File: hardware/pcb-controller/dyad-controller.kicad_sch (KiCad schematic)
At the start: 41 parts, among them J1 USB_C_Receptacle_USB2.0, J10 USB-C split link, J2 SWD, J6 HC-FPC-0.5-20P-FH20, J7 HC-FPC-0.5-20P-FH20, J8 HC-FPC-0.5-14P-FH20, J9 USB-C split link, SW1 BOOTSEL, SW2 RESET, U1 W25Q128JVS, U2 USBLC6-2SC6, U3 RP2040, U4 XC6206PxxxMR-Regulator_Linear, Y1 12MHz

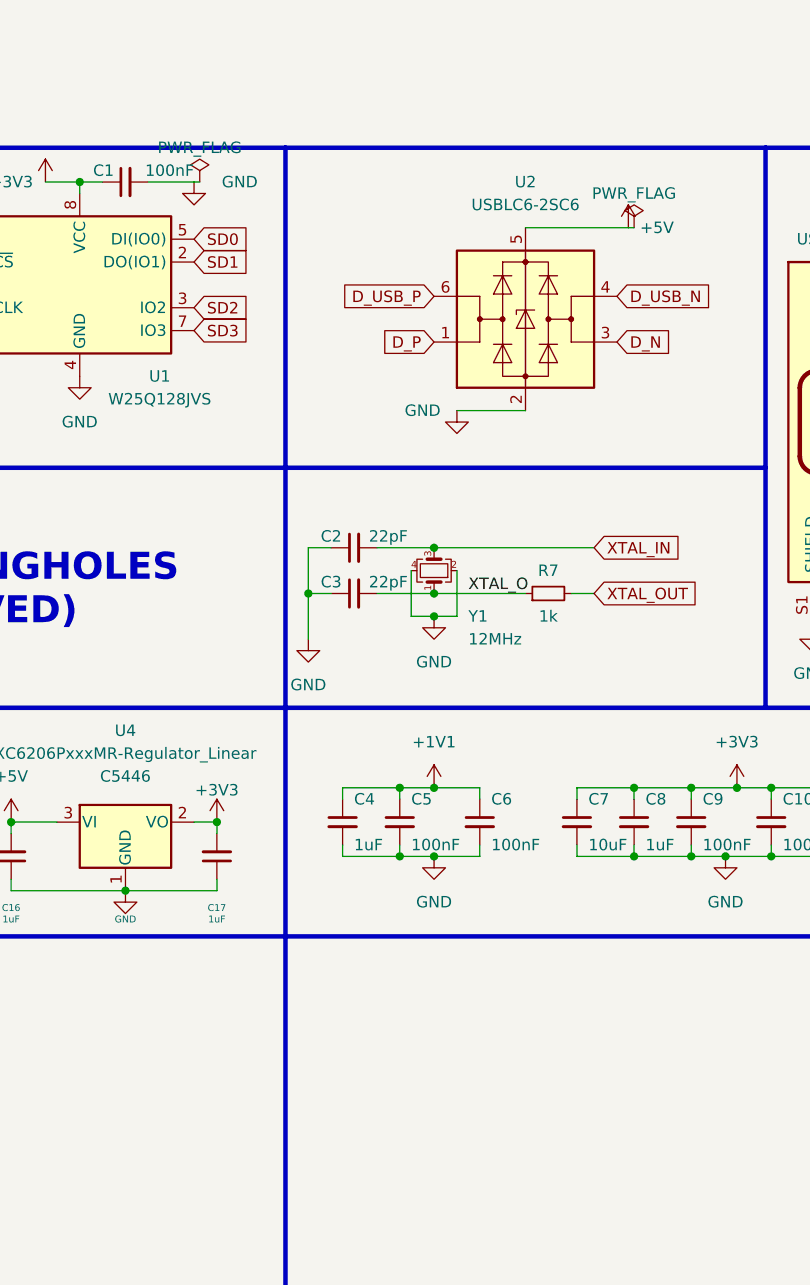
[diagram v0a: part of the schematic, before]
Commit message: Swap the controller crystal to the RP2040 minimal design's ABM8-272-T3
Found by the CONTROLLER.md §6 checklist, item 3. The reference design's
crystal was LCSC C9002 (YXC X322512MSB4SI): CL 20 pF and ESR 80 ohm,
loaded with 22 pF caps. That gives ~11 + 3 pF stray = ~14 pF against the
20 pF it needs, so it would run fast; and its ESR is above the 50 ohm that
Hardware design with RP2040 §2.3 assumes when sizing the 1 kOhm XOUT
resistor, so start-up margin was unknown. The guide says any other crystal
circuit "will require extensive testing".

Now the guide's circuit unchanged: Abracon ABM8-272-T3 (LCSC C20625731,
CL 10 pF, ESR <= 50 ohm) with two 15 pF C0G caps (C2/C3, LCSC C1548, JLCPCB
Basic) and R7 at 1 kOhm -- 7.5 pF + ~3 pF stray = 10.5 pF.

Same 3.2 x 2.5 mm 4-pad package with crystal on pins 1/3 and ground on
2/4, so the footprint and routing are untouched; only Y1's LCSC and
description and C2/C3's value and LCSC change, mirrored onto the board
footprints. CONTROLLER.md's BOM and §4 "transfers unchanged" list updated.

ERC unchanged at 152. DRC: 0 errors, 0 unconnected. Parity: 14.

Co-Authored-By: Claude Opus 5.5 <noreply@anthropic.com>
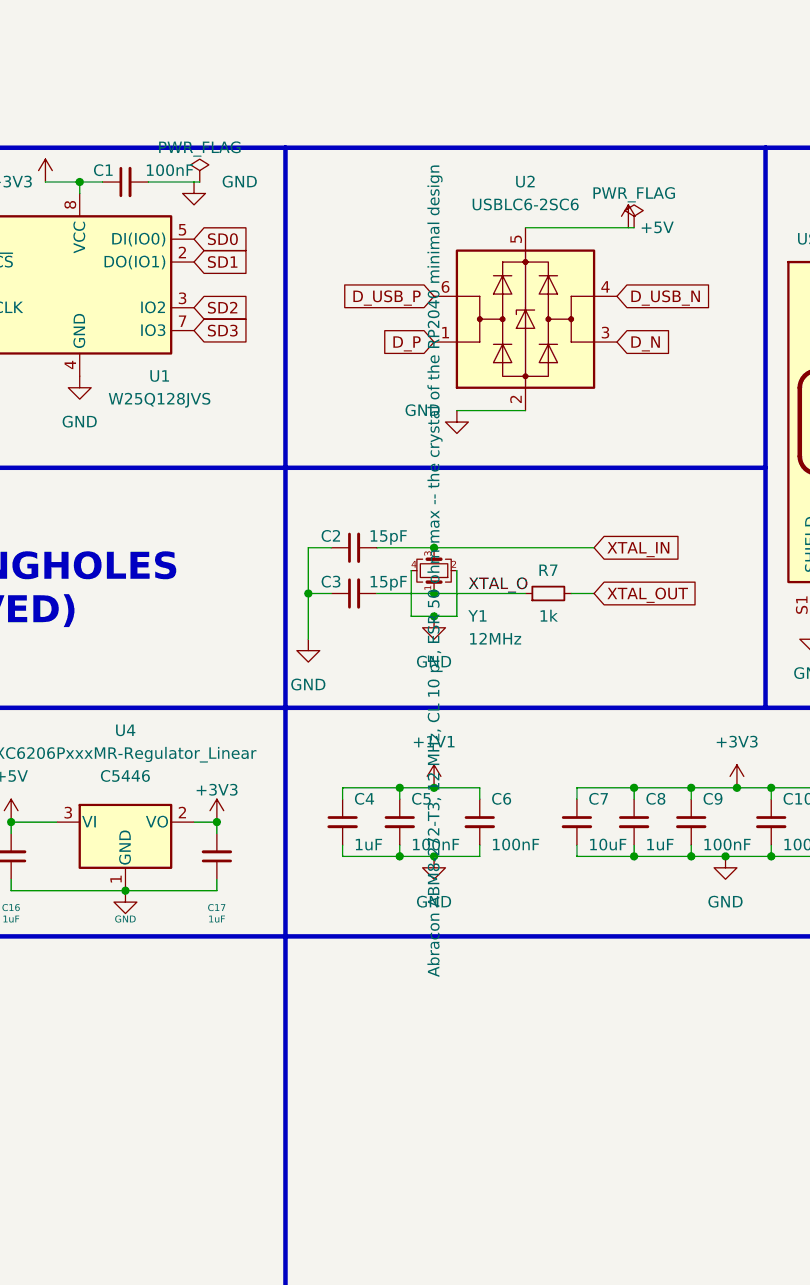
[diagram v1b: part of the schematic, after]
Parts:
- C2, C3: value 22pF -> 15pF; LCSC C1555 -> C1548
- Y1: LCSC C9002 -> C20625731
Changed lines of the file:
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@@
 			)
 		)
-		(property "Value" "22pF"
+		(property "Value" "15pF"
 			(at 187.325 62.23 90)
 			(show_name no)
@@
 			)
 		)
-		(property "LCSC" "C1555"
+		(property "LCSC" "C1548"
 			(at 183.515 63.5 0)
 			(hide yes)
@@
 			)
 		)
-		(property "Value" "22pF"
+		(property "Value" "15pF"
 			(at 187.325 57.15 90)
 			(show_name no)
@@
 			)
 		)
-		(property "LCSC" "C1555"
+		(property "LCSC" "C1548"
 			(at 183.515 58.42 0)
 			(hide yes)
@@
 			)
 		)
-		(property "Description" ""
+		(property "Description" "Abracon ABM8-272-T3, 12 MHz, CL 10 pF, ESR 50 ohm max -- the crystal of the RP2040 minimal design"
 			(at 192.405 60.96 0)
 			(show_name no)
@@
 			)
 		)
-		(property "LCSC" "C9002"
+		(property "LCSC" "C20625731"
 			(at 192.405 60.96 0)
 			(hide yes)

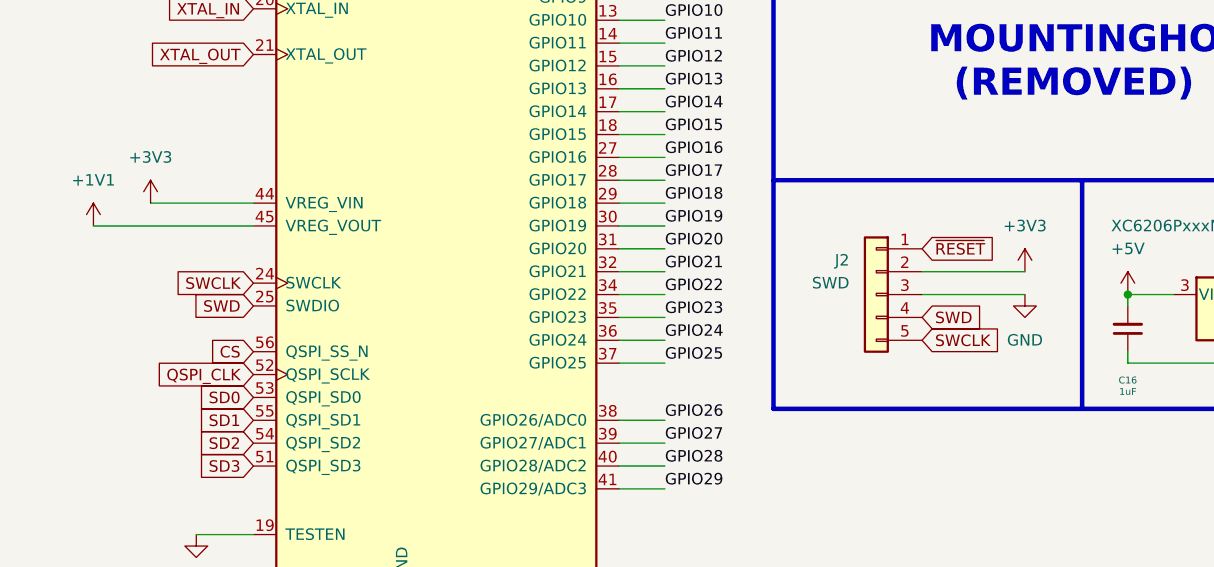
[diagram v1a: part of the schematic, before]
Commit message: Remove the SWD header, move the RP2040 block forward, reroute with USB on B.Cu
The §6 checklist failed item 5: D+ 18 mm, D- 26 mm, six vias. Several
attempts to reroute USB in place left gaps, because the corridor from J1 to
U3 had no room for the nets that have to hop beside the pair.

- J2 (1x05 SWD socket, 13.8 x 3.6 mm through-hole) removed from schematic
  and board, with its wiring, labels and power symbols; U3's SWCLK/SWDIO
  get no-connect flags. Flashing is over USB with BOOTSEL. ERC 152 -> 145,
  no new findings.
- U3 with all its decoupling, the crystal network, R5/R6 and the flash
  with C1/R1 moved 4 mm forward as one group into the freed space; U2 a
  further 1 mm so a via fits beside its +5V pin, which sits between its
  two USB pins.
- USB routed by hand-written router on B.Cu: D+ 15.9 mm, D- 16.1 mm, no
  vias. The rest by Freerouting around it; then +5V to U2 and one GPIO1
  hop at J7 routed by the same router, 11 vias moved for hole spacing, a
  VBUS track at J1 necked to 0.3 mm, GND fills with 76 stitching vias, C13's
  GND pad solid. JLC marker moved clear of C15.

Against 2dc9af0: total track 2,167 -> 1,915 mm; F.Cu fill 48% in 5 pieces
-> 46% in 4, largest 656 -> 774 mm^2; B.Cu 47% in 16 -> 49% in 9, largest
738 -> 803 mm^2. Ground under USB 4% -> 9%, crystal 42% -> 27%, QSPI 26% ->
1% -- the matrix bundle still crosses beneath them on F.Cu.

CONTROLLER.md: J2's removal recorded, and the §6 checklist results added
(items 1-3, 8 pass; 4, 5 partial; 6, 7 open), with a correction to the
claim that no matrix crosses this board.

DRC: 0 errors, 0 unconnected. Parity: 14 field-copy differences.

Co-Authored-By: Claude Opus 5.5 <noreply@anthropic.com>
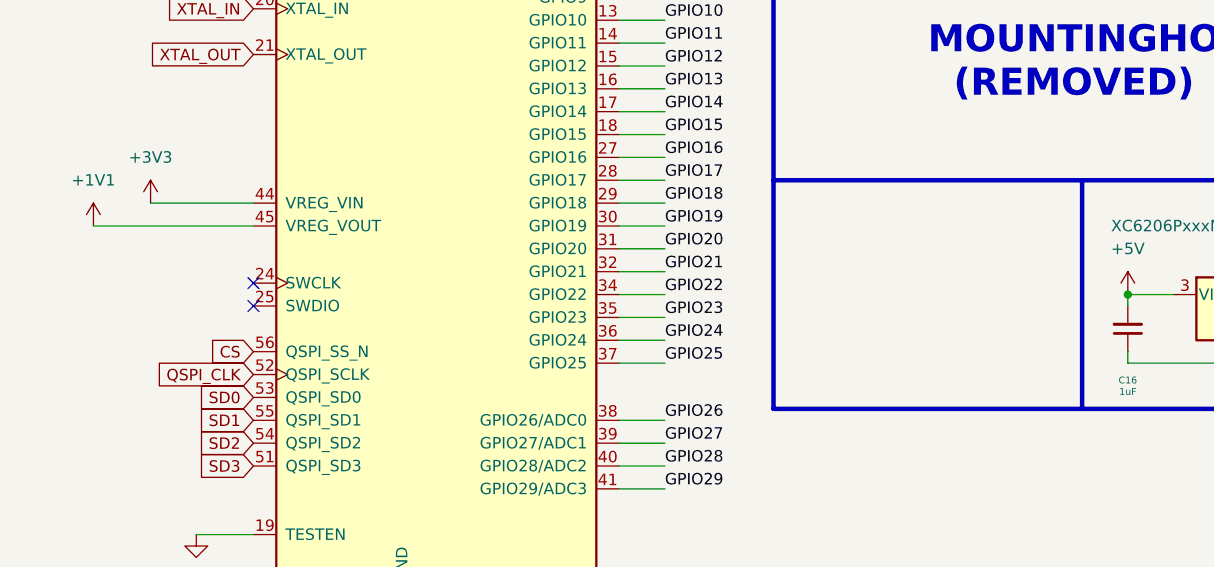
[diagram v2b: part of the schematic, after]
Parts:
- removed J2: SWD, Connector_PinSocket_2.54mm:PinSocket_1x05_P2.54mm_Vertical, symbol Connector_Generic:Conn_01x05
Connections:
- net SWCLK: no longer names the net of U3.24 (SWCLK)
- net SWD: no longer names the net of U3.25 (SWDIO)
- no-connect marks 14 -> 16

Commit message: Give the split USB-C ports J9/J10 their LCSC number
Found while exporting the assembly BOM: J9 and J10 had no LCSC field, so
JLCPCB would have left the split-link USB-C ports unplaced on both halves.
They are the same HRO TYPE-C-31-M-12 as J1 (CONTROLLER.md §3), C165948.
Added to the schematic symbols and mirrored onto the board footprints.

ERC unchanged at 145. DRC: 0 errors, 0 unconnected. Parity: 14.

Co-Authored-By: Claude Opus 5.5 <noreply@anthropic.com>
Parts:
- J10, J9: LCSC (none) -> C165948
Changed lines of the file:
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@@
+			)
+		)
+		(property "LCSC" "C165948"
+			(at 241.935 44.45 0)
+			(hide yes)
+			(show_name no)
+			(do_not_autoplace no)
+			(effects
+				(font
+					(size 1.27 1.27)
+				)
 			)
 		)
@@
 			(effects
 				(font
+					(size 1.27 1.27)
+				)
+			)
+		)
+		(property "LCSC" "C165948"
+			(at 241.935 44.45 0)
+			(hide yes)
+			(show_name no)
+			(do_not_autoplace no)
+			(effects
+				(font
